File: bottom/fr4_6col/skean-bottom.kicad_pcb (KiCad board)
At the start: 2 copper layers, 153.2 x 95.3 mm, 10 parts

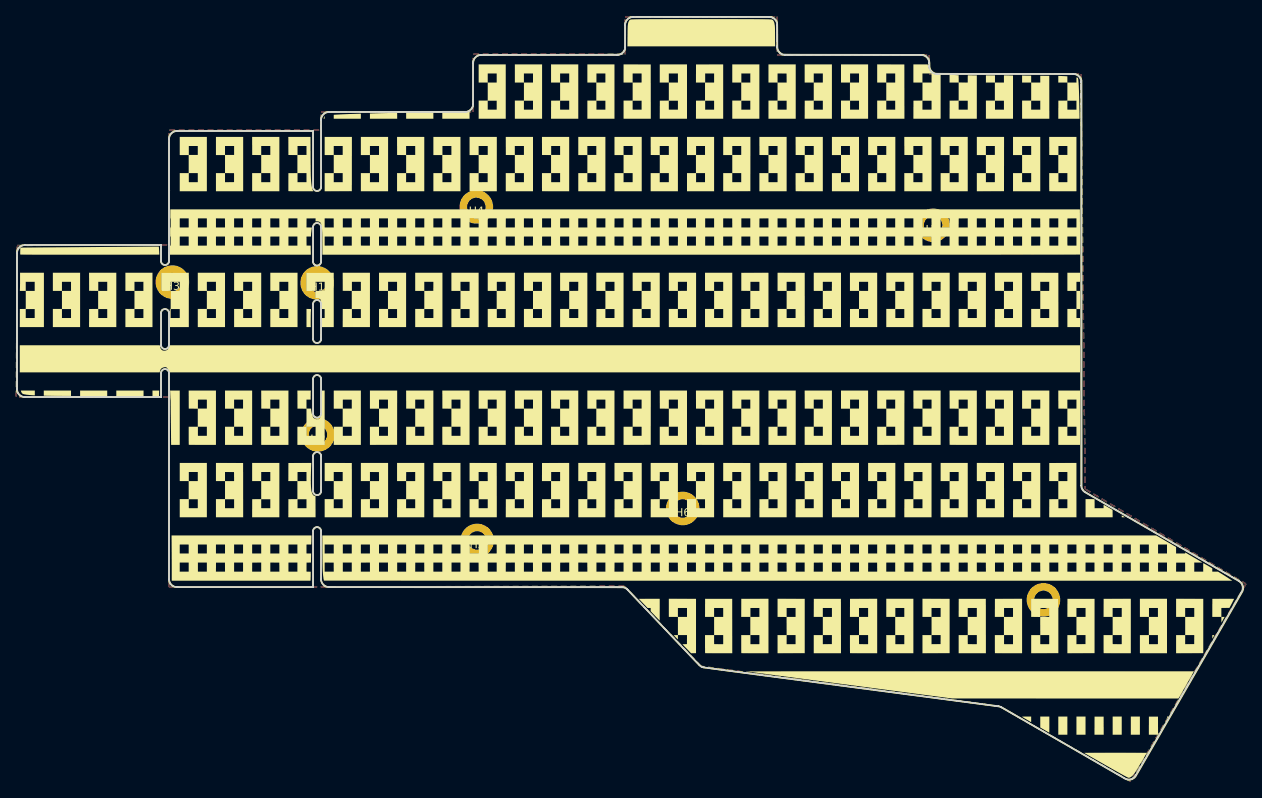
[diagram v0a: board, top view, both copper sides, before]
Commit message: Bottom and plate versions
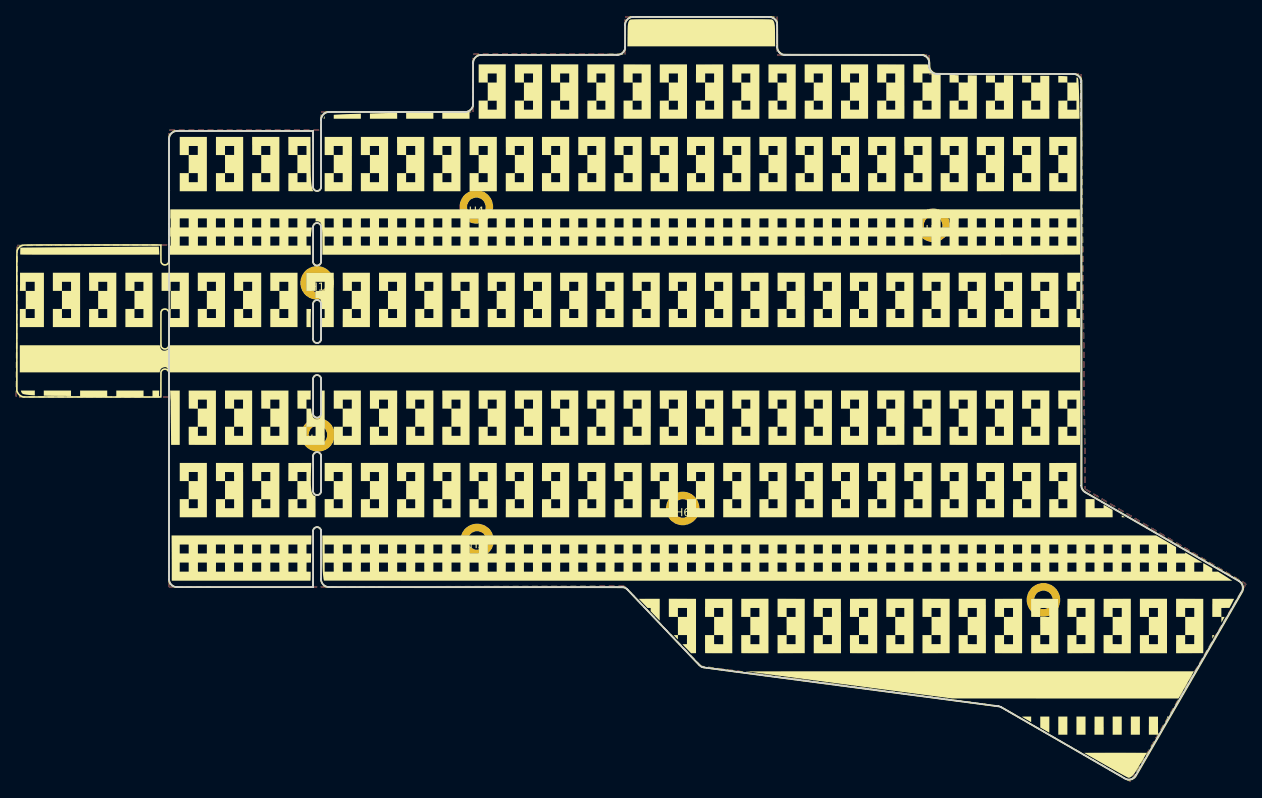
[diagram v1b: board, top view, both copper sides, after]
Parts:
- removed H3: MountingHole, kbd:M2_Hole_TH
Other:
- board size 153.2 x 95.3 mm -> 134.2 x 95.3 mm

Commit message: V0.3 case files
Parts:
- removed the G*** at (90.8, 62.0) (x2)
- removed H6: MountingHole, kbd:M2_Hole_TH
- added G***: LOGO, Silks:skean_truchet_6col_back, F.Cu at (100.1, 61.6)
- added G***: LOGO, Silks:skean_truchet_6col, F.Cu at (100.1, 61.6)
- added REF**: Bumpon_REV, kbd:Bumpon_REV, F.Cu at (39.7, 35.1)
- added REF**: Bumpon_REV, kbd:Bumpon_REV, F.Cu at (140.7, 28.0)
- added REF**: Bumpon_REV, kbd:Bumpon_REV, F.Cu at (155.4, 94.4)
- added REF**: Bumpon_REV, kbd:Bumpon_REV, F.Cu at (39.7, 79.1)
- added REF**: Bumpon_REV, kbd:Bumpon_REV, F.Cu at (99.7, 20.8)
- added REF**: Bumpon_REV, kbd:Bumpon_REV, F.Cu at (103.2, 89.1)
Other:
- outline, holes or cut-outs redrawn
